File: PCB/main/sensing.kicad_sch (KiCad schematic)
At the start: 13 parts, among them IC1 LM358DT

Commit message: changes made to all
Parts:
- renumbered C2 to C10, C1 to C9, R7 to R10, R8 to R11, R1 to R4, R2 to R5, R3 to R6, R4 to R7, R5 to R8, R6 to R9
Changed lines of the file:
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@@
   (symbol (lib_id "SamacSys_Parts:RC0603FR-071KL") (at 160.02 140.97 0) (unit 1)
     (in_bom yes) (on_board yes)
-    (property "Reference" "R8" (id 0) (at 168.91 140.97 0))
+    (property "Reference" "R11" (id 0) (at 168.91 140.97 0))
     (property "Value" "RC0603FR-071KL" (id 1) (at 171.45 144.78 0))
     (property "Footprint" "SamacSys_Parts:RESC1608X55N" (id 2) (at 173.99 139.7 0)
@@
   (symbol (lib_id "power:GND") (at 158.75 160.02 0) (unit 1)
     (in_bom yes) (on_board yes) (fields_autoplaced)
-    (property "Reference" "#PWR06" (id 0) (at 158.75 166.37 0)
+    (property "Reference" "#PWR034" (id 0) (at 158.75 166.37 0)
       (effects (font (size 1.27 1.27)) hide)
     )
@@
   (symbol (lib_id "SamacSys_Parts:RC0603FR-071KL") (at 154.94 114.3 270) (unit 1)
     (in_bom yes) (on_board yes)
-    (property "Reference" "R5" (id 0) (at 154.94 123.19 0))
+    (property "Reference" "R8" (id 0) (at 154.94 123.19 0))
     (property "Value" "RC0603FR-071KL" (id 1) (at 157.48 121.92 0))
     (property "Footprint" "SamacSys_Parts:RESC1608X55N" (id 2) (at 156.21 128.27 0)
@@
   (symbol (lib_id "SamacSys_Parts:CL10A105KB8NNNC") (at 82.55 133.35 270) (unit 1)
     (in_bom yes) (on_board yes)
-    (property "Reference" "C1" (id 0) (at 82.55 137.16 90)
+    (property "Reference" "C9" (id 0) (at 82.55 137.16 90)
       (effects (font (size 1.27 1.27)) (justify left))
     )
@@
   (symbol (lib_id "power:GND") (at 113.03 151.13 0) (unit 1)
     (in_bom yes) (on_board yes) (fields_autoplaced)
-    (property "Reference" "#PWR05" (id 0) (at 113.03 157.48 0)
+    (property "Reference" "#PWR033" (id 0) (at 113.03 157.48 0)
       (effects (font (size 1.27 1.27)) hide)
     )
@@
   (symbol (lib_id "SamacSys_Parts:RC0603FR-071KL") (at 158.75 114.3 0) (unit 1)
     (in_bom yes) (on_board yes)
-    (property "Reference" "R6" (id 0) (at 167.64 114.3 0))
+    (property "Reference" "R9" (id 0) (at 167.64 114.3 0))
     (property "Value" "RC0603FR-071KL" (id 1) (at 167.64 116.84 0))
     (property "Footprint" "SamacSys_Parts:RESC1608X55N" (id 2) (at 172.72 113.03 0)
@@
   (symbol (lib_id "SamacSys_Parts:AC0402FR-07536KL") (at 74.93 133.35 270) (unit 1)
     (in_bom yes) (on_board yes)
-    (property "Reference" "R3" (id 0) (at 73.66 140.97 90)
+    (property "Reference" "R6" (id 0) (at 73.66 140.97 90)
       (effects (font (size 1.27 1.27)) (justify left))
     )
@@
   (symbol (lib_id "SamacSys_Parts:RC0603FR-071KL") (at 158.75 140.97 270) (unit 1)
     (in_bom yes) (on_board yes)
-    (property "Reference" "R7" (id 0) (at 157.48 148.59 90)
+    (property "Reference" "R10" (id 0) (at 157.48 148.59 90)
       (effects (font (size 1.27 1.27)) (justify left))
     )
@@
   (symbol (lib_id "power:GND") (at 82.55 151.13 0) (unit 1)
     (in_bom yes) (on_board yes) (fields_autoplaced)
-    (property "Reference" "#PWR03" (id 0) (at 82.55 157.48 0)
+    (property "Reference" "#PWR031" (id 0) (at 82.55 157.48 0)
       (effects (font (size 1.27 1.27)) hide)
     )
@@
   (symbol (lib_id "power:GND") (at 25.4 157.48 0) (unit 1)
     (in_bom yes) (on_board yes) (fields_autoplaced)
-    (property "Reference" "#PWR01" (id 0) (at 25.4 163.83 0)
+    (property "Reference" "#PWR029" (id 0) (at 25.4 163.83 0)
       (effects (font (size 1.27 1.27)) hide)
     )
@@
   (symbol (lib_id "power:GND") (at 246.38 130.81 0) (mirror y) (unit 1)
     (in_bom yes) (on_board yes) (fields_autoplaced)
-    (property "Reference" "#PWR07" (id 0) (at 246.38 137.16 0)
+    (property "Reference" "#PWR035" (id 0) (at 246.38 137.16 0)
       (effects (font (size 1.27 1.27)) hide)
     )
@@
   (symbol (lib_id "SamacSys_Parts:RC0603FR-071KL") (at 25.4 134.62 270) (mirror x) (unit 1)
     (in_bom yes) (on_board yes)
-    (property "Reference" "R1" (id 0) (at 25.4 125.73 0))
+    (property "Reference" "R4" (id 0) (at 25.4 125.73 0))
     (property "Value" "RC0603FR-071KL" (id 1) (at 22.86 125.73 0))
     (property "Footprint" "SamacSys_Parts:RESC1608X55N" (id 2) (at 26.67 120.65 0)
@@
   (symbol (lib_id "SamacSys_Parts:RC0603FR-071KL") (at 25.4 154.94 270) (mirror x) (unit 1)
     (in_bom yes) (on_board yes)
-    (property "Reference" "R2" (id 0) (at 25.4 146.05 0))
+    (property "Reference" "R5" (id 0) (at 25.4 146.05 0))
     (property "Value" "RC0603FR-071KL" (id 1) (at 22.86 146.05 0))
     (property "Footprint" "SamacSys_Parts:RESC1608X55N" (id 2) (at 26.67 140.97 0)
@@
   (symbol (lib_id "power:PWR_FLAG") (at 73.66 152.4 90) (unit 1)
     (in_bom yes) (on_board yes) (fields_autoplaced)
-    (property "Reference" "#FLG01" (id 0) (at 71.755 152.4 0)
+    (property "Reference" "#FLG04" (id 0) (at 71.755 152.4 0)
       (effects (font (size 1.27 1.27)) hide)
     )
@@
   (symbol (lib_id "SamacSys_Parts:CL10A105KB8NNNC") (at 113.03 133.35 270) (unit 1)
     (in_bom yes) (on_board yes)
-    (property "Reference" "C2" (id 0) (at 115.57 139.7 90)
+    (property "Reference" "C10" (id 0) (at 115.57 139.7 90)
       (effects (font (size 1.27 1.27)) (justify left))
     )
@@
   (symbol (lib_id "SamacSys_Parts:AC0402FR-07536KL") (at 105.41 133.35 270) (unit 1)
     (in_bom yes) (on_board yes)
-    (property "Reference" "R4" (id 0) (at 104.14 140.97 90)
+    (property "Reference" "R7" (id 0) (at 104.14 140.97 90)
       (effects (font (size 1.27 1.27)) (justify left))
     )
@@
   (symbol (lib_id "power:PWR_FLAG") (at 276.86 124.46 90) (unit 1)
     (in_bom yes) (on_board yes) (fields_autoplaced)
-    (property "Reference" "#FLG02" (id 0) (at 274.955 124.46 0)
+    (property "Reference" "#FLG05" (id 0) (at 274.955 124.46 0)
       (effects (font (size 1.27 1.27)) hide)
     )
@@
   (symbol (lib_id "power:GND") (at 74.93 153.67 0) (unit 1)
     (in_bom yes) (on_board yes) (fields_autoplaced)
-    (property "Reference" "#PWR02" (id 0) (at 74.93 160.02 0)
+    (property "Reference" "#PWR030" (id 0) (at 74.93 160.02 0)
       (effects (font (size 1.27 1.27)) hide)
     )
@@
   (symbol (lib_id "power:GND") (at 105.41 153.67 0) (unit 1)
     (in_bom yes) (on_board yes) (fields_autoplaced)
-    (property "Reference" "#PWR04" (id 0) (at 105.41 160.02 0)
-      (effects (font (size 1.27 1.27)) hide)
-    )
+    (property "Reference" "#PWR032" (id 0) (at 105.41 160.02 0)
+      (effects (font (size 1.27 1.27)) hide)
+    )

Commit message: git main schematics updated
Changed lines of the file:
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@@
   (junction (at 82.55 133.35) (diameter 0) (color 0 0 0 0)
   )
-  (junction (at 276.86 124.46) (diameter 0) (color 0 0 0 0)
-  )
   (junction (at 74.93 133.35) (diameter 0) (color 0 0 0 0)
   )
@@
   (junction (at 113.03 133.35) (diameter 0) (color 0 0 0 0)
   )
-  (junction (at 74.93 152.4) (diameter 0) (color 0 0 0 0)
-  )
   (junction (at 105.41 133.35) (diameter 0) (color 0 0 0 0)
   )
@@
     (stroke (width 0) (type default) (color 0 0 0 0))
   )
-  (wire (pts (xy 74.93 152.4) (xy 74.93 151.13))
-    (stroke (width 0) (type default) (color 0 0 0 0))
-  )
   (wire (pts (xy 177.8 140.97) (xy 179.07 140.97))
     (stroke (width 0) (type default) (color 0 0 0 0))
@@
     (stroke (width 0) (type default) (color 0 0 0 0))
   )
-  (wire (pts (xy 74.93 153.67) (xy 74.93 152.4))
-    (stroke (width 0) (type default) (color 0 0 0 0))
-  )
-  (wire (pts (xy 276.86 114.3) (xy 276.86 124.46))
+  (wire (pts (xy 74.93 151.13) (xy 74.93 153.67))
+    (stroke (width 0) (type default) (color 0 0 0 0))
+  )
+  (wire (pts (xy 276.86 114.3) (xy 276.86 132.08))
     (stroke (width 0) (type default) (color 0 0 0 0))
   )
@@
   )
   (wire (pts (xy 245.11 123.19) (xy 246.38 123.19))
-    (stroke (width 0) (type default) (color 0 0 0 0))
-  )
-  (wire (pts (xy 276.86 124.46) (xy 276.86 132.08))
-    (stroke (width 0) (type default) (color 0 0 0 0))
-  )
-  (wire (pts (xy 73.66 152.4) (xy 74.93 152.4))
     (stroke (width 0) (type default) (color 0 0 0 0))
   )
@@
     (pin "2")
   )
-  (symbol (lib_id "power:PWR_FLAG") (at 73.66 152.4 90) (unit 1)
-    (in_bom yes) (on_board yes) (fields_autoplaced)
-    (property "Reference" "#FLG04" (id 0) (at 71.755 152.4 0)
-      (effects (font (size 1.27 1.27)) hide)
-    )
-    (property "Value" "PWR_FLAG" (id 1) (at 69.85 152.3999 90)
-      (effects (font (size 1.27 1.27)) (justify left))
-    )
-    (property "Footprint" "" (id 2) (at 73.66 152.4 0)
-      (effects (font (size 1.27 1.27)) hide)
-    )
-    (property "Datasheet" "~" (id 3) (at 73.66 152.4 0)
-      (effects (font (size 1.27 1.27)) hide)
-    )
-    (pin "1")
-  )
   (symbol (lib_id "SamacSys_Parts:CL10A105KB8NNNC") (at 113.03 133.35 270) (unit 1)
     (in_bom yes) (on_board yes)
@@
     (pin "2")
   )
-  (symbol (lib_id "power:PWR_FLAG") (at 276.86 124.46 90) (unit 1)
-    (in_bom yes) (on_board yes) (fields_autoplaced)
-    (property "Reference" "#FLG05" (id 0) (at 274.955 124.46 0)
-      (effects (font (size 1.27 1.27)) hide)
-    )
-    (property "Value" "PWR_FLAG" (id 1) (at 273.05 124.4599 90)
-      (effects (font (size 1.27 1.27)) (justify left))
-    )
-    (property "Footprint" "" (id 2) (at 276.86 124.46 0)
-      (effects (font (size 1.27 1.27)) hide)
-    )
-    (property "Datasheet" "~" (id 3) (at 276.86 124.46 0)
-      (effects (font (size 1.27 1.27)) hide)
-    )
-    (pin "1")
-  )
   (symbol (lib_id "power:GND") (at 74.93 153.67 0) (unit 1)

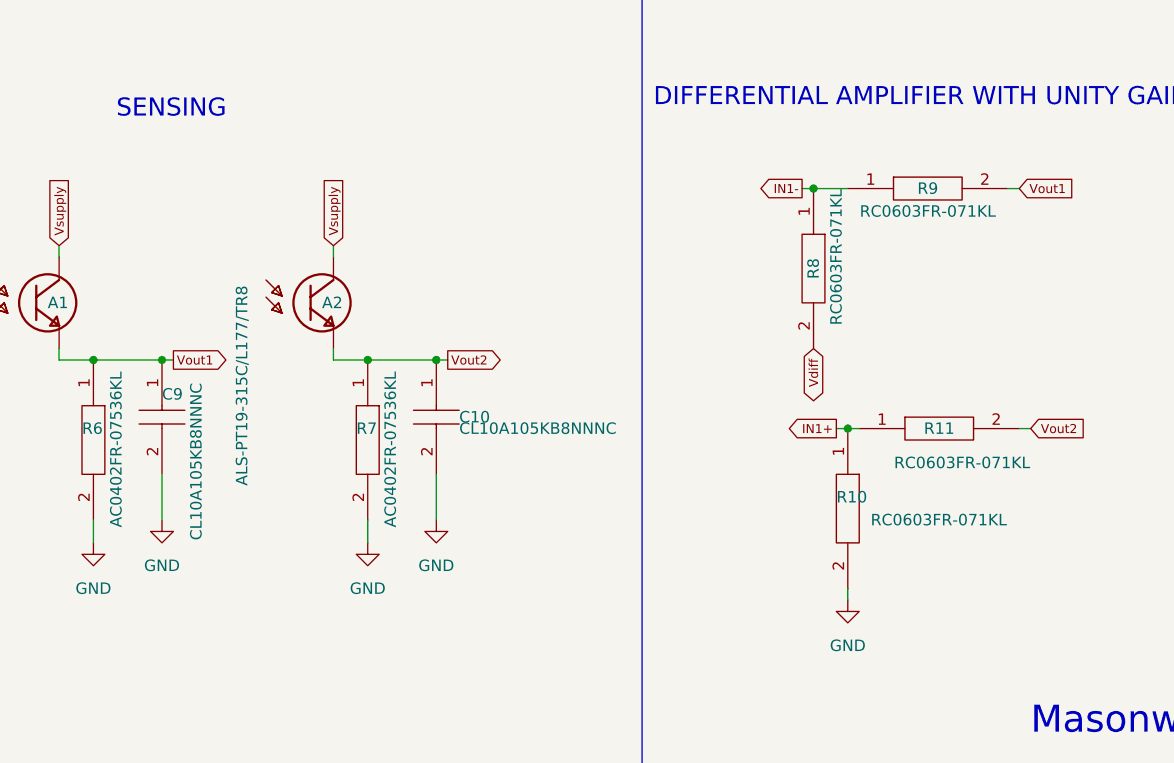
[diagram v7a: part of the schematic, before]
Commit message: added more test points
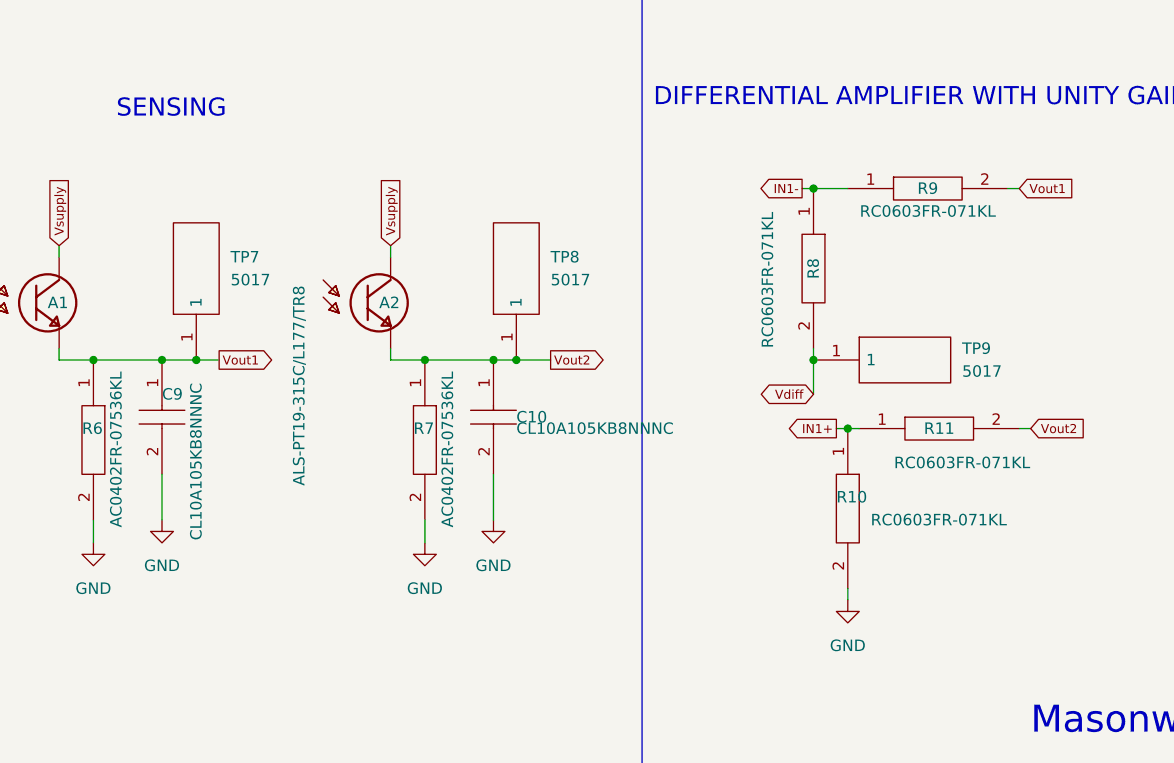
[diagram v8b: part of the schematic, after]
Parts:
- added TP7, TP8, TP9: 5017, 5017, symbol SamacSys_Parts_power:5017
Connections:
- net Vdiff: now also TP9.1
- net Vout1: now also TP7.1
- net Vout2: now also TP8.1
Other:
- moved on the sheet: A2, C10, R7
